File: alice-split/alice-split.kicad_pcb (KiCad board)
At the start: 2 copper layers, 0 parts

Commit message: Drew curved traces instead of the usual defaults. Not sure I like it. Going to branch and try again.
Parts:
- added D1: D_Small, Diode_SMD:D_1206_3216Metric, B.Cu at (83.8, 53.8)
- added D10: D_Small, Diode_SMD:D_1206_3216Metric, B.Cu at (183.4, 59.9)
- added D11: D_Small, Diode_SMD:D_1206_3216Metric, B.Cu at (164.6, 55.9)
- added D12: D_Small, Diode_SMD:D_1206_3216Metric, B.Cu at (144.8, 53.3)
- added D13: D_Small, Diode_SMD:D_1206_3216Metric, B.Cu at (126.0, 55.9)
- added D14: D_Small, Diode_SMD:D_1206_3216Metric, B.Cu at (107.2, 55.9)
- added D15: D_Small, Diode_SMD:D_1206_3216Metric, B.Cu at (107.7, 74.7)
- added D16: D_Small, Diode_SMD:D_1206_3216Metric, B.Cu at (131.1, 75.2)
- added D17: D_Small, Diode_SMD:D_1206_3216Metric, B.Cu at (151.9, 72.4)
- added D18: D_Small, Diode_SMD:D_1206_3216Metric, B.Cu at (170.4, 76.5)
- added D19: D_Small, Diode_SMD:D_1206_3216Metric, B.Cu at (189.0, 80.3)
- added D2: D_Small, Diode_SMD:D_1206_3216Metric, F.Cu at (-86.4, 63.0)
- added D20: D_Small, Diode_SMD:D_1206_3216Metric, B.Cu at (207.8, 84.3)
- added D21: D_Small, Diode_SMD:D_1206_3216Metric, B.Cu at (100.8, 94.0)
- added D22: D_Small, Diode_SMD:D_1206_3216Metric, B.Cu at (131.8, 93.7)
- added D23: D_Small, Diode_SMD:D_1206_3216Metric, B.Cu at (153.2, 92.5)
- added D24: D_Small, Diode_SMD:D_1206_3216Metric, B.Cu at (170.9, 95.5)
- added D25: D_Small, Diode_SMD:D_1206_3216Metric, B.Cu at (189.7, 99.8)
- added D26: D_Small, Diode_SMD:D_1206_3216Metric, B.Cu at (208.5, 104.1)
- added D27: D_Small, Diode_SMD:D_1206_3216Metric, B.Cu at (114.8, 103.1)
- added D28: D_Small, Diode_SMD:D_1206_3216Metric, B.Cu at (137.4, 112.8)
- added D29: D_Small, Diode_SMD:D_1206_3216Metric, B.Cu at (157.7, 112.8)
- added D3: D_Small, Diode_SMD:D_1206_3216Metric, F.Cu at (-79.1, 141.7)
- added D30: D_Small, Diode_SMD:D_1206_3216Metric, B.Cu at (176.5, 116.6)
- added D31: D_Small, Diode_SMD:D_1206_3216Metric, B.Cu at (195.1, 120.7)
- added D32: D_Small, Diode_SMD:D_1206_3216Metric, B.Cu at (213.9, 124.5)
- added D33: D_Small, Diode_SMD:D_1206_3216Metric, B.Cu at (99.3, 131.8)
- added D34: D_Small, Diode_SMD:D_1206_3216Metric, B.Cu at (118.1, 131.8)
- added D35: D_Small, Diode_SMD:D_1206_3216Metric, B.Cu at (153.2, 132.6)
- added D36: D_Small, Diode_SMD:D_1206_3216Metric, B.Cu at (174.2, 136.9)
- added D37: D_Small, Diode_SMD:D_1206_3216Metric, B.Cu at (217.9, 145.0)
- added D4: D_Small, Diode_SMD:D_1206_3216Metric, F.Cu at (-79.1, 145.1)
- added D5: D_Small, Diode_SMD:D_1206_3216Metric, F.Cu at (-79.1, 148.5)
- added D6: D_Small, Diode_SMD:D_1206_3216Metric, F.Cu at (-79.1, 151.9)
- added D7: D_Small, Diode_SMD:D_1206_3216Metric, F.Cu at (-77.2, 120.4)
- added D8: D_Small, Diode_SMD:D_1206_3216Metric, B.Cu at (221.0, 67.6)
- added D9: D_Small, Diode_SMD:D_1206_3216Metric, B.Cu at (202.7, 64.0)
- added SW38: SW_PUSH-MX_W_LED, SofleRGB:SK6812MINI_and_cherry, F.Cu at (-251.0, 57.5)
- added SW39: SW_PUSH-MX_W_LED, SofleRGB:SK6812MINI_and_cherry, F.Cu at (-210.7, 117.3)
- added SW40: SW_PUSH-MX_W_LED, SofleRGB:SK6812MINI_and_cherry, F.Cu at (-268.0, 89.5)
- added SW41: SW_PUSH-MX_W_LED, SofleRGB:SK6812MINI_and_cherry, F.Cu at (-329.3, 121.5)
- added SW42: SW_PUSH-MX_W_LED, SofleRGB:SK6812MINI_and_cherry, F.Cu at (-329.3, 137.0)
- added SW43: SW_PUSH-MX_W_LED, SofleRGB:SK6812MINI_and_cherry, F.Cu at (-329.3, 152.5)
- added SW44: SW_PUSH-MX_W_LED, SofleRGB:SK6812MINI_and_cherry, F.Cu at (-353.4, 162.8)
- added SW45: SW_PUSH-MX_W_LED, SofleRGB:SK6812MINI_and_cherry, F.Cu at (-353.4, 178.3)
- added SW46: SW_PUSH-MX_W_LED, SofleRGB:SK6812MINI_and_cherry, F.Cu at (-353.4, 193.8)
- added SW47: SW_PUSH-MX_W_LED, SofleRGB:SK6812MINI_and_cherry, F.Cu at (-353.4, 209.3)
- added SW48: SW_PUSH-MX_W_LED, SofleRGB:SK6812MINI_and_cherry, F.Cu at (-353.4, 224.8)
- added SW49: SW_PUSH-MX_W_LED, SofleRGB:SK6812MINI_and_cherry, F.Cu at (-198.6, 76.2)
- added SW50: SW_PUSH-MX_W_LED, SofleRGB:SK6812MINI_and_cherry, F.Cu at (-299.1, 134.0)
- added SW51: SW_PUSH-MX_W_LED, SofleRGB:SK6812MINI_and_cherry, F.Cu at (-299.1, 149.5)
- added SW52: SW_PUSH-MX_W_LED, SofleRGB:SK6812MINI_and_cherry, F.Cu at (-299.1, 165.0)
- added SW53: SW_PUSH-MX_W_LED, SofleRGB:SK6812MINI_and_cherry, F.Cu at (-299.1, 180.5)
- added SW54: SW_PUSH-MX_W_LED, SofleRGB:SK6812MINI_and_cherry, F.Cu at (-299.1, 196.0)
- added SW55: SW_PUSH-MX_W_LED, SofleRGB:SK6812MINI_and_cherry, F.Cu at (-299.1, 211.5)
- added SW56: SW_PUSH-MX_W_LED, SofleRGB:SK6812MINI_and_cherry, F.Cu at (-299.1, 227.0)
- added SW57: SW_PUSH-MX_W_LED, SofleRGB:SK6812MINI_and_cherry, F.Cu at (-299.1, 242.5)
- added SW58: SW_PUSH-MX_W_LED, SofleRGB:SK6812MINI_and_cherry, F.Cu at (-299.1, 258.0)
- added SW59: SW_PUSH-MX_W_LED, SofleRGB:SK6812MINI_and_cherry, F.Cu at (-299.1, 273.5)
- added SW60: SW_PUSH-MX_W_LED, SofleRGB:SK6812MINI_and_cherry, F.Cu at (-281.8, 118.5)
- added SW61: SW_PUSH-MX_W_LED, SofleRGB:SK6812MINI_and_cherry, F.Cu at (-281.8, 134.0)
- added SW62: SW_PUSH-MX_W_LED, SofleRGB:SK6812MINI_and_cherry, F.Cu at (-281.8, 149.5)
- added SW63: SW_PUSH-MX_W_LED, SofleRGB:SK6812MINI_and_cherry, F.Cu at (-281.8, 165.0)
- added SW64: SW_PUSH-MX_W_LED, SofleRGB:SK6812MINI_and_cherry, F.Cu at (-281.8, 180.5)
- added SW65: SW_PUSH-MX_W_LED, SofleRGB:SK6812MINI_and_cherry, F.Cu at (-281.8, 196.0)
- added SW66: SW_PUSH-MX_W_LED, SofleRGB:SK6812MINI_and_cherry, F.Cu at (-281.8, 211.5)
- added SW67: SW_PUSH-MX_W_LED, SofleRGB:SK6812MINI_and_cherry, F.Cu at (-281.8, 227.0)
- added SW68: SW_PUSH-MX_W_LED, SofleRGB:SK6812MINI_and_cherry, F.Cu at (-281.8, 242.5)
- added SW69: SW_PUSH-MX_W_LED, SofleRGB:SK6812MINI_and_cherry, F.Cu at (-281.8, 258.0)
- added SW70: SW_PUSH-MX_W_LED, SofleRGB:SK6812MINI_and_cherry, F.Cu at (-281.8, 273.5)
- added SW71: SW_PUSH-MX_W_LED, SofleRGB:SK6812MINI_and_cherry, F.Cu at (-264.5, 118.5)
- added SW72: SW_PUSH-MX_W_LED, SofleRGB:SK6812MINI_and_cherry, F.Cu at (-264.5, 134.0)
- added SW73: SW_PUSH-MX_W_LED, SofleRGB:SK6812MINI_and_cherry, F.Cu at (-264.5, 149.5)
- added SW74: SW_PUSH-MX_W_LED, SofleRGB:SK6812MINI_and_cherry, F.Cu at (-264.5, 165.0)
- added SW75: SW_PUSH-MX_W_LED, SofleRGB:SK6812MINI_and_cherry, F.Cu at (-264.5, 180.5)
- added SW76: SW_PUSH-MX_W_LED, SofleRGB:SK6812MINI_and_cherry, F.Cu at (-264.5, 196.0)
- added SW77: SW_PUSH-MX_W_LED, SofleRGB:SK6812MINI_and_cherry, F.Cu at (-264.5, 211.5)
- added SW78: SW_PUSH-MX_W_LED, SofleRGB:SK6812MINI_and_cherry, F.Cu at (-264.5, 227.0)
- added SW79: SW_PUSH-MX_W_LED, SofleRGB:SK6812MINI_and_cherry, F.Cu at (-264.5, 242.5)
- added SW80: SW_PUSH-MX_W_LED, SofleRGB:SK6812MINI_and_cherry, F.Cu at (-264.5, 258.0)
- added SW81: SW_PUSH-MX_W_LED, SofleRGB:SK6812MINI_and_cherry, F.Cu at (-192.9, 259.5)
- added SW82: SW_PUSH-MX_W_LED, SofleRGB:SK6812MINI_and_cherry, F.Cu at (-228.0, 130.5)
- added SW83: SW_PUSH-MX_W_LED, SofleRGB:SK6812MINI_and_cherry, F.Cu at (-228.0, 146.0)
- added SW84: SW_PUSH-MX_W_LED, SofleRGB:SK6812MINI_and_cherry, F.Cu at (-228.0, 161.5)
- added SW85: SW_PUSH-MX_W_LED, SofleRGB:SK6812MINI_and_cherry, F.Cu at (-228.0, 177.0)
- added SW86: SW_PUSH-MX_W_LED, SofleRGB:SK6812MINI_and_cherry, F.Cu at (-228.0, 192.5)
- added SW87: SW_PUSH-MX_W_LED, SofleRGB:SK6812MINI_and_cherry, F.Cu at (-228.0, 208.0)
- added SW88: SW_PUSH-MX_W_LED, SofleRGB:SK6812MINI_and_cherry, F.Cu at (-228.0, 223.5)
- added SW89: SW_PUSH-MX_W_LED, SofleRGB:SK6812MINI_and_cherry, F.Cu at (-228.0, 239.0)
- added SW_1: SW_PUSH-MX_W_LED, SofleRGB:SK6812MINI_and_cherry, F.Cu at (134.0, 54.4)
- added SW_2: SW_PUSH-MX_W_LED, SofleRGB:SK6812MINI_and_cherry, F.Cu at (152.6, 52.2)
- added SW_3: SW_PUSH-MX_W_LED, SofleRGB:SK6812MINI_and_cherry, F.Cu at (173.1, 56.2)
- added SW_4: SW_PUSH-MX_W_LED, SofleRGB:SK6812MINI_and_cherry, F.Cu at (191.8, 60.2)
- added SW_5: SW_PUSH-MX_W_LED, SofleRGB:SK6812MINI_and_cherry, F.Cu at (210.4, 64.1)
- added SW_6: SW_PUSH-MX_W_LED, SofleRGB:SK6812MINI_and_cherry, F.Cu at (229.0, 68.1)
- added SW_A1: SW_PUSH-MX_W_LED, SofleRGB:SK6812MINI_and_cherry, F.Cu at (140.0, 92.5)
- added SW_B_L1: SW_PUSH-MX_W_LED, SofleRGB:SK6812MINI_and_cherry, F.Cu at (221.8, 125.0)
- added SW_C1: SW_PUSH-MX_W_LED, SofleRGB:SK6812MINI_and_cherry, F.Cu at (184.6, 117.0)
- added SW_CAPS1: SW_PUSH-MX_W_LED, SofleRGB:SK6812MINI_and_cherry, F.Cu at (109.1, 92.5)
- added SW_CTRL_L1: SW_PUSH-MX_W_LED, SofleRGB:SK6812MINI_and_cherry, F.Cu at (107.3, 130.6)
- added SW_D1: SW_PUSH-MX_W_LED, SofleRGB:SK6812MINI_and_cherry, F.Cu at (178.8, 96.0)
- added SW_E1: SW_PUSH-MX_W_LED, SofleRGB:SK6812MINI_and_cherry, F.Cu at (178.5, 76.8)
- added SW_ESC1: SW_PUSH-MX_W_LED, SofleRGB:SK6812MINI_and_cherry, F.Cu at (91.9, 52.2)
- added SW_F1: SW_PUSH-MX_W_LED, SofleRGB:SK6812MINI_and_cherry, F.Cu at (-113.1, -344.2)
- added SW_F2: SW_PUSH-MX_W_LED, SofleRGB:SK6812MINI_and_cherry, F.Cu at (-53.7, -218.7)
- added SW_F3: SW_PUSH-MX_W_LED, SofleRGB:SK6812MINI_and_cherry, F.Cu at (29.0, -292.6)
- added SW_F4: SW_PUSH-MX_W_LED, SofleRGB:SK6812MINI_and_cherry, F.Cu at (60.5, -290.6)
- added SW_F5: SW_PUSH-MX_W_LED, SofleRGB:SK6812MINI_and_cherry, F.Cu at (91.4, -280.9)
- added SW_F6: SW_PUSH-MX_W_LED, SofleRGB:SK6812MINI_and_cherry, F.Cu at (59.4, -248.4)
- added SW_F7: SW_PUSH-MX_W_LED, SofleRGB:SK6812MINI_and_cherry, F.Cu at (-59.8, -186.2)
- added SW_F8: SW_PUSH-MX_W_LED, SofleRGB:SK6812MINI_and_cherry, F.Cu at (197.6, 100.1)
- added SW_FN1: SW_PUSH-MX_W_LED, SofleRGB:SK6812MINI_and_cherry, F.Cu at (225.9, 145.3)
- added SW_G1: SW_PUSH-MX_W_LED, SofleRGB:SK6812MINI_and_cherry, F.Cu at (216.4, 104.3)
- added SW_M1: SW_PUSH-MX_W_LED, SofleRGB:SK6812MINI_and_cherry, F.Cu at (-15.4, 25.5)
- added SW_M2: SW_PUSH-MX_W_LED, SofleRGB:SK6812MINI_and_cherry, F.Cu at (-15.4, 41.0)
- added SW_MOD_L1: SW_PUSH-MX_W_LED, SofleRGB:SK6812MINI_and_cherry, F.Cu at (161.1, 133.0)
- added SW_OPT1: SW_PUSH-MX_W_LED, SofleRGB:SK6812MINI_and_cherry, F.Cu at (126.4, 130.6)
- added SW_Q1: SW_PUSH-MX_W_LED, SofleRGB:SK6812MINI_and_cherry, F.Cu at (139.3, 73.4)
- added SW_R1: SW_PUSH-MX_W_LED, SofleRGB:SK6812MINI_and_cherry, F.Cu at (197.1, 80.8)
- added SW_S1: SW_PUSH-MX_W_LED, SofleRGB:SK6812MINI_and_cherry, F.Cu at (161.0, 93.0)
- added SW_SHIFT_L1: SW_PUSH-MX_W_LED, SofleRGB:SK6812MINI_and_cherry, F.Cu at (114.5, 111.5)
- added SW_SPC_L1: SW_PUSH-MX_W_LED, SofleRGB:SK6812MINI_and_cherry, F.Cu at (195.5, 138.9)
- added SW_T1: SW_PUSH-MX_W_LED, SofleRGB:SK6812MINI_and_cherry, F.Cu at (215.8, 84.7)
- added SW_TAB1: SW_PUSH-MX_W_LED, SofleRGB:SK6812MINI_and_cherry, F.Cu at (115.5, 73.4)
- added SW_TILDE1: SW_PUSH-MX_W_LED, SofleRGB:SK6812MINI_and_cherry, F.Cu at (115.0, 54.4)
- added SW_V1: SW_PUSH-MX_W_LED, SofleRGB:SK6812MINI_and_cherry, F.Cu at (203.1, 121.0)
- added SW_W1: SW_PUSH-MX_W_LED, SofleRGB:SK6812MINI_and_cherry, F.Cu at (159.8, 72.8)
- added SW_X1: SW_PUSH-MX_W_LED, SofleRGB:SK6812MINI_and_cherry, F.Cu at (165.9, 113.1)
- added SW_Z1: SW_PUSH-MX_W_LED, SofleRGB:SK6812MINI_and_cherry, F.Cu at (145.4, 111.5)
- added U1: Sparkfun_Pro_Micro, Keebio-Parts:ArduinoProMicro, B.Cu at (230.4, 47.2)
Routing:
- net Net-(D16-A): track 0.00 -> 3.47 mm
- net Net-(D1-A): track 0.00 -> 3.24 mm
- net Net-(D10-A): track 0.00 -> 3.22 mm
- net Net-(D21-A): track 0.00 -> 3.21 mm
- net Net-(D11-A): track 0.00 -> 3.17 mm
- net Net-(D13-A): track 0.00 -> 3.09 mm
- net Net-(D26-A): track 0.00 -> 3.06 mm
- net Net-(D9-A): track 0.00 -> 3.03 mm
- net Net-(D29-A): track 0.00 -> 3.03 mm
- net Net-(D14-A): track 0.00 -> 3.01 mm
- net Net-(D37-A): track 0.00 -> 2.98 mm
- net Net-(D25-A): track 0.00 -> 2.97 mm
- net Net-(D34-A): track 0.00 -> 2.94 mm
- net Net-(D18-A): track 0.00 -> 2.94 mm
- net Net-(D31-A): track 0.00 -> 2.94 mm
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
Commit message: Redid the traces but with the usual 45 degree traces. Looks nicer, made more progress.
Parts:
- moved SW_F1 368.9 mm to (-381.5, -91.0)
- moved SW_F3 368.9 mm to (-239.4, -39.4)
- moved SW_F4 368.9 mm to (-207.9, -37.4)
- moved SW_F2 368.9 mm to (-322.0, 34.5)
- moved SW_F5 368.9 mm to (-176.9, -27.7)
- moved SW_F6 368.9 mm to (-208.9, 4.80)
- moved SW_F7 368.9 mm to (-328.1, 67.0)
- moved SW_TILDE1 140.1 mm to (-18.0, 10.3)
- moved D14 132.7 mm to (-21.6, 23.9)
- moved SW_M1 112.9 mm to (87.8, 71.3)
- moved SW_M2 110.7 mm to (83.7, 90.4)
- moved D1 23.1 mm to (106.9, 56.0)
- moved SW_ESC1 23.1 mm to (115.0, 54.4)
- moved D36 13.4 mm to (187.5, 139.2), turned to 78 degrees
- moved U1 0.57 mm to (230.9, 47.0)
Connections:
- D1 pad 1: ROW5 -> ROW4
- D14 pad 1: ROW4 -> unconnected-(D14-K-Pad1)
- D14 pad 2: Net-(D14-A) -> unconnected-(D14-A-Pad2)
- D2 pad 1: ROW5 -> unconnected-(D2-K-Pad1)
- D3 pad 1: ROW5 -> unconnected-(D3-K-Pad1)
- D4 pad 1: ROW5 -> unconnected-(D4-K-Pad1)
- D5 pad 1: ROW5 -> unconnected-(D5-K-Pad1)
- D6 pad 1: ROW5 -> unconnected-(D6-K-Pad1)
- D7 pad 1: ROW5 -> unconnected-(D7-K-Pad1)
- SW_E1 pad 4: Net-(SW_6B-DIN) -> VDD
- SW_ESC1 pad 3: Net-(SW_ESC1B-DIN) -> Net-(SW_1B-DOUT)
- SW_ESC1 pad 6: COL15 -> COL14
- SW_F1 pad 1: Net-(SW_ESC1B-DIN) -> unconnected-(SW_F1B-DOUT-Pad1)
- SW_F1 pad 2: VCC -> unconnected-(SW_F1B-VSS-Pad2)
- SW_F1 pad 4: VDD -> unconnected-(SW_F1B-VDD-Pad4)
- SW_F1 pad 6: COL13 -> unconnected-(SW_F1-Pad6)
- SW_F2 pad 2: VCC -> unconnected-(SW_F2B-VSS-Pad2)
- SW_F2 pad 4: VDD -> unconnected-(SW_F2B-VDD-Pad4)
- SW_F2 pad 6: COL12 -> unconnected-(SW_F2-Pad6)
- SW_F3 pad 2: VCC -> unconnected-(SW_F3B-VSS-Pad2)
- SW_F3 pad 4: VDD -> unconnected-(SW_F3B-VDD-Pad4)
- SW_F3 pad 6: COL11 -> unconnected-(SW_F3-Pad6)
- SW_F4 pad 2: VCC -> unconnected-(SW_F4B-VSS-Pad2)
- SW_F4 pad 4: VDD -> unconnected-(SW_F4B-VDD-Pad4)
- SW_F4 pad 6: COL10 -> unconnected-(SW_F4-Pad6)
- SW_F5 pad 2: VCC -> unconnected-(SW_F5B-VSS-Pad2)
- SW_F5 pad 4: VDD -> unconnected-(SW_F5B-VDD-Pad4)
- SW_F5 pad 6: COL9 -> unconnected-(SW_F5-Pad6)
- SW_F6 pad 2: VCC -> unconnected-(SW_F6B-VSS-Pad2)
- SW_F6 pad 3: Net-(SW_F6B-DIN) -> unconnected-(SW_F6B-DIN-Pad3)
- SW_F6 pad 4: VDD -> unconnected-(SW_F6B-VDD-Pad4)
- SW_F6 pad 6: COL8 -> unconnected-(SW_F6-Pad6)
- SW_Q1 pad 4: Net-(SW_6B-DIN) -> VDD
- SW_R1 pad 4: Net-(SW_6B-DIN) -> VDD
- SW_TAB1 pad 4: Net-(SW_6B-DIN) -> VDD
- SW_TILDE1 pad 1: Net-(SW_F6B-DIN) -> unconnected-(SW_TILDE1B-DOUT-Pad1)
- SW_TILDE1 pad 2: VCC -> unconnected-(SW_TILDE1B-VSS-Pad2)
- SW_TILDE1 pad 3: Net-(SW_1B-DOUT) -> unconnected-(SW_TILDE1B-DIN-Pad3)
- SW_TILDE1 pad 4: VDD -> unconnected-(SW_TILDE1B-VDD-Pad4)
- SW_TILDE1 pad 5: Net-(D14-A) -> unconnected-(SW_TILDE1-Pad5)
- SW_TILDE1 pad 6: COL14 -> unconnected-(SW_TILDE1-Pad6)
- SW_W1 pad 4: Net-(SW_6B-DIN) -> VDD
- U1 pad 10: ROW4 -> unconnected-(U1-D7-Pad10)
- U1 pad 11: ROW5 -> unconnected-(U1-D8/A8-Pad11)
- U1 pad 12: ROW6 -> unconnected-(U1-~D9/A9-Pad12)
- U1 pad 13: COL15 -> unconnected-(U1-~D10/A10-Pad13)
- U1 pad 23: VDD -> unconnected-(U1-GND-Pad23)
- U1 pad 3: unconnected-(U1-GND-Pad3) -> VDD
- U1 pad 4: unconnected-(U1-GND-Pad4) -> VDD
- U1 pad 5: unconnected-(U1-D2-Pad5) -> ROW0
- U1 pad 6: ROW0 -> ROW1
- U1 pad 7: ROW1 -> ROW2
- U1 pad 8: ROW2 -> ROW3
- U1 pad 9: ROW3 -> ROW4
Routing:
- net VDD: track 0.00 -> 675.7 mm, vias 0 -> 31
- net VCC: track 0.00 -> 663.5 mm
- net COL14: track 0.00 -> 222.5 mm, vias 0 -> 5
- net ROW1: track 0.00 -> 195.8 mm
- net COL13: track 0.00 -> 194.1 mm, vias 0 -> 5
- net ROW2: track 0.00 -> 186.7 mm
- net ROW3: track 0.00 -> 170.7 mm
- net ROW4: track 0.00 -> 162.8 mm
- net COL11: track 0.00 -> 162.3 mm, vias 0 -> 5
- net Net-(SW_G1B-DIN): track 0.00 -> 158.5 mm
- net Net-(SW_6B-DIN): track 0.00 -> 151.4 mm
- net Net-(SW_B_L1B-DIN): track 0.00 -> 146.3 mm
- net COL12: track 0.00 -> 144.9 mm, vias 0 -> 4
- net Net-(SW_CAPS1B-DOUT): track 0.00 -> 143.5 mm
- net COL10: track 0.00 -> 135.0 mm, vias 0 -> 5
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
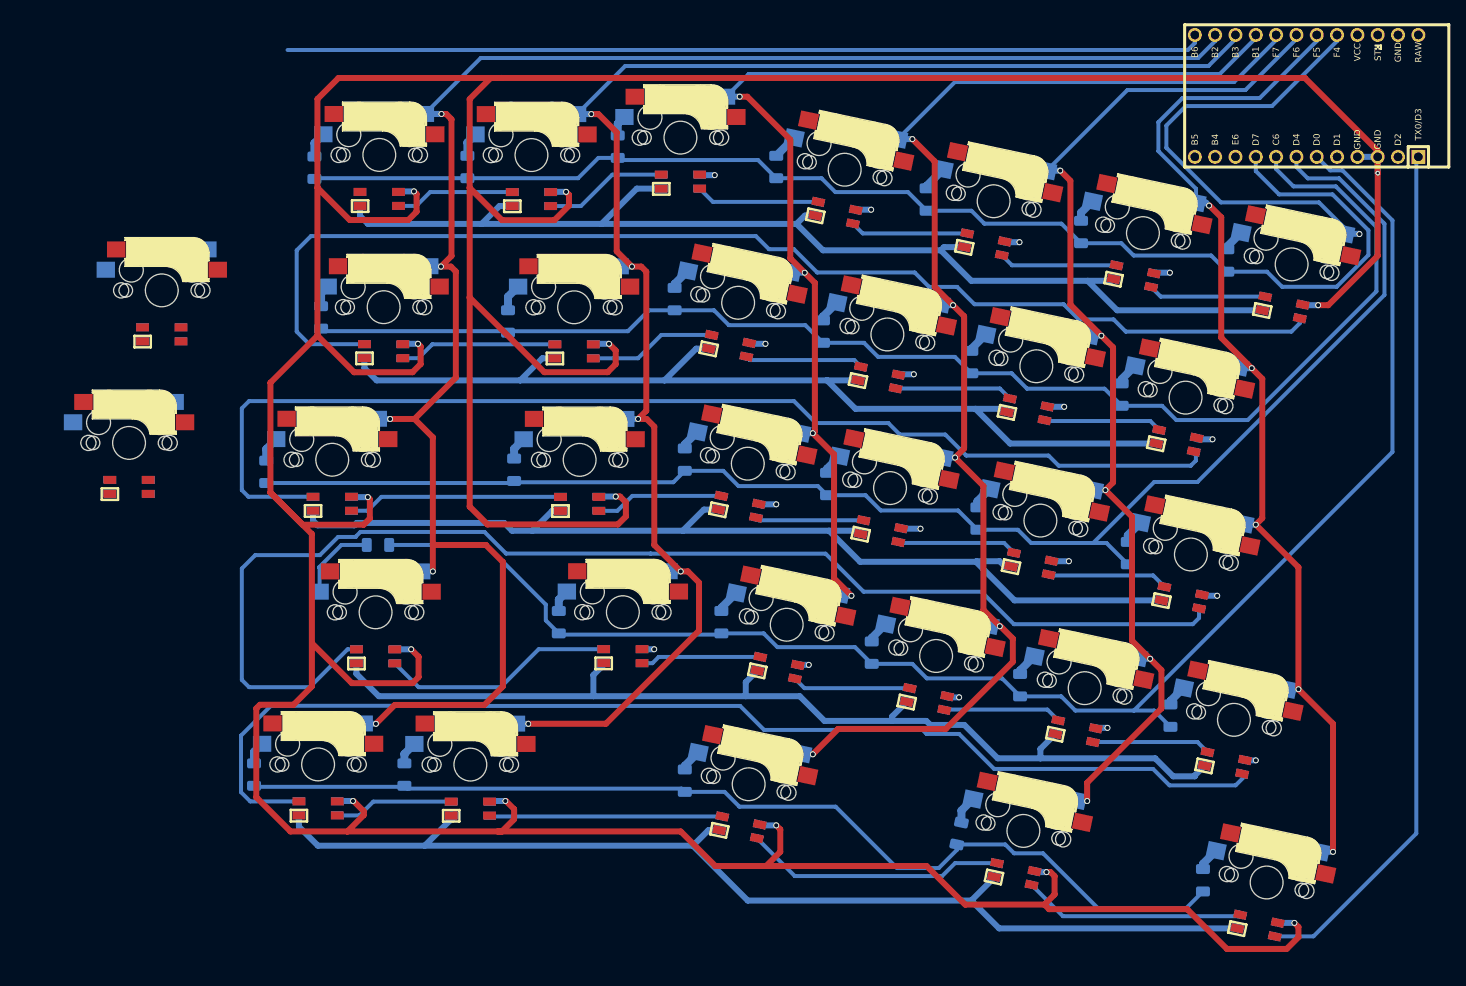
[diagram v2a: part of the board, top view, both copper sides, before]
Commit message: Added encoder and macro keys. Whole lefthand side is wired. Needs another review.
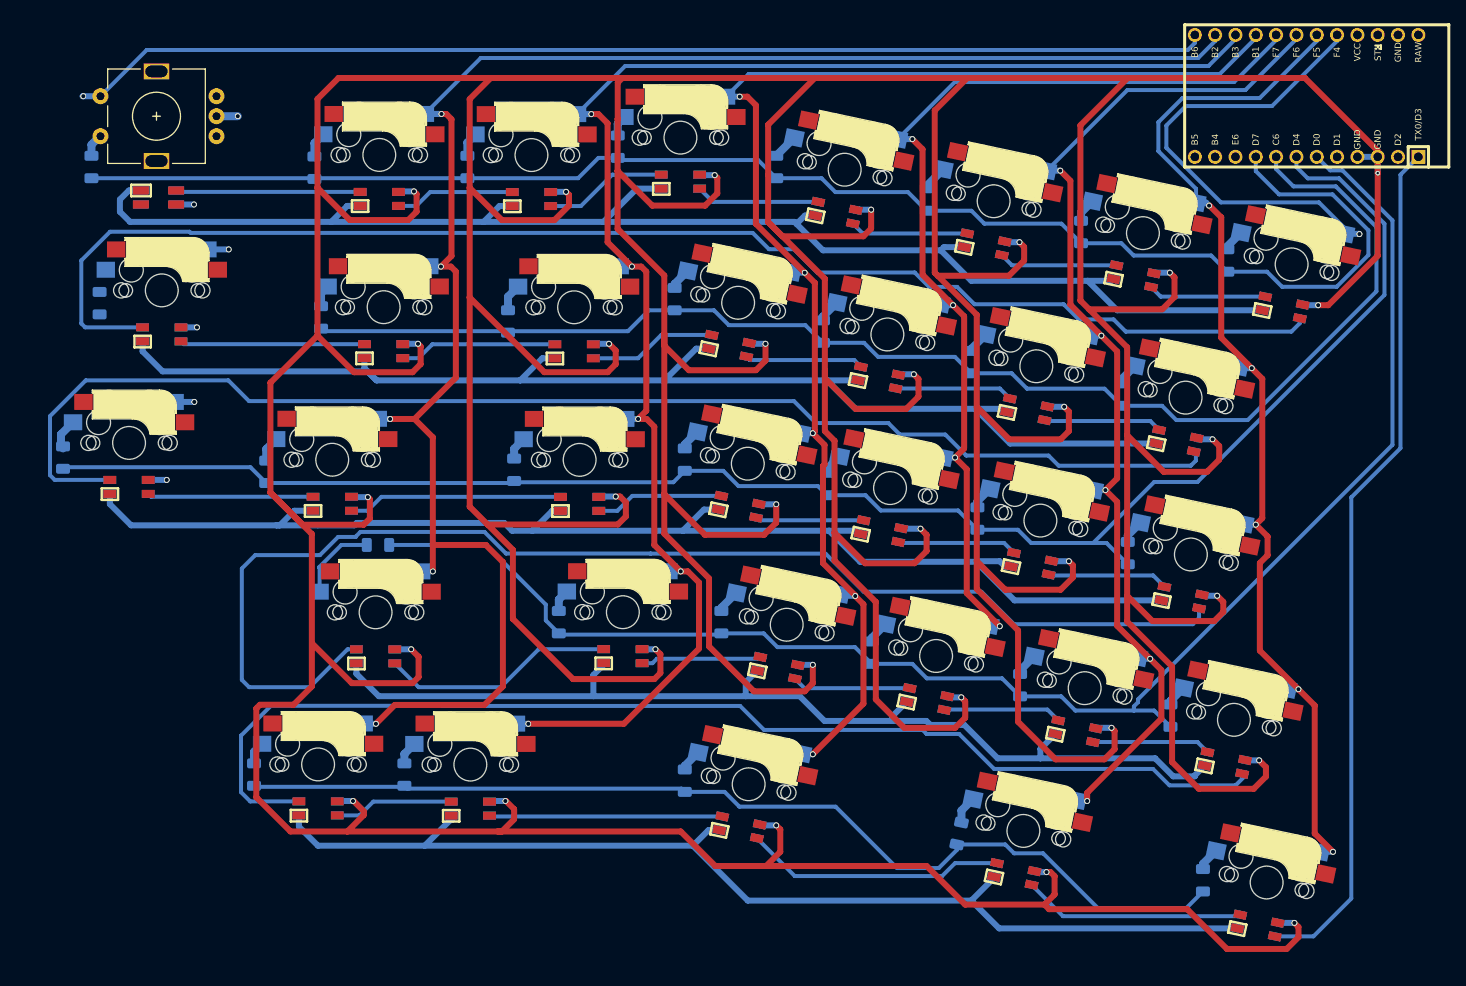
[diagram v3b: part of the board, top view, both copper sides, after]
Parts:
- added D38: D_Small, Diode_SMD:D_1206_3216Metric, B.Cu at (79.0, 55.9)
- added D39: D_Small, Diode_SMD:D_1206_3216Metric, B.Cu at (80.0, 72.9)
- added D40: D_Small, Diode_SMD:D_1206_3216Metric, B.Cu at (75.4, 92.2)
- added D41: LED_sk2812_SM, SofleRGB:SK6812MINI_underglow_dev, F.Cu at (87.4, 59.7)
- added SW1: RotaryEncoder_Switch, SofleRGB:RotaryEncoder_Alps_EC11E-Switch_Vertical_H20mm-keebio_modified, F.Cu at (87.1, 49.5)
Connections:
- SW_ESC1 pad 1: unconnected-(SW_ESC1B-DOUT-Pad1) -> Net-(D41-DIN)
- SW_M1 pad 1: unconnected-(SW_M1B-DOUT-Pad1) -> Net-(SW_6B-DIN)
- SW_M1 pad 2: unconnected-(SW_M1B-VSS-Pad2) -> VCC
- SW_M1 pad 3: unconnected-(SW_M1B-DIN-Pad3) -> Net-(SW_M1B-DIN)
- SW_M1 pad 4: unconnected-(SW_M1B-VDD-Pad4) -> VDD
- SW_M1 pad 5: unconnected-(SW_M1-Pad5) -> Net-(D39-A)
- SW_M1 pad 6: unconnected-(SW_M1-Pad6) -> COL15
- SW_M2 pad 1: unconnected-(SW_M2B-DOUT-Pad1) -> Net-(SW_M2B-DOUT)
- SW_M2 pad 2: unconnected-(SW_M2B-VSS-Pad2) -> VCC
- SW_M2 pad 3: unconnected-(SW_M2B-DIN-Pad3) -> Net-(SW_CAPS1B-DOUT)
- SW_M2 pad 4: unconnected-(SW_M2B-VDD-Pad4) -> VDD
- SW_M2 pad 5: unconnected-(SW_M2-Pad5) -> Net-(D40-A)
- SW_M2 pad 6: unconnected-(SW_M2-Pad6) -> COL15
- SW_MOD_L1 pad 6: COL11 -> COL12
- SW_T1 pad 3: Net-(SW_CAPS1B-DOUT) -> Net-(SW_M2B-DOUT)
- SW_TAB1 pad 1: Net-(SW_6B-DIN) -> Net-(SW_M1B-DIN)
- U1 pad 11: unconnected-(U1-D8/A8-Pad11) -> ENCA
- U1 pad 12: unconnected-(U1-~D9/A9-Pad12) -> ENCB
- U1 pad 13: unconnected-(U1-~D10/A10-Pad13) -> COL15
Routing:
- net VDD: track 675.7 -> 1335.6 mm, vias 31 -> 35
- net Net-(SW_M2B-DOUT): track 0.00 -> 165.7 mm
- net COL15: track 0.00 -> 147.9 mm, vias 0 -> 3
- net Net-(SW_CAPS1B-DOUT): track 143.5 -> 20.7 mm
- net unconnected-(U1-~D10/A10-Pad13): track 114.8 -> 0.00 mm
- net VCC: track 663.5 -> 764.4 mm
- net COL11: track 162.3 -> 125.8 mm, vias 5 -> 4
- net ROW4: track 162.8 -> 190.7 mm
- net ROW2: track 186.7 -> 213.0 mm
- net COL12: track 144.9 -> 170.1 mm, vias 4 -> 5
- net Net-(SW_6B-DIN): track 151.4 -> 175.8 mm
- net Net-(SW_M1B-DIN): track 0.00 -> 23.1 mm
- net Net-(D41-DIN): track 0.00 -> 23.1 mm
- net Net-(D40-A): track 0.00 -> 4.00 mm
- net ENC_S2: track 0.00 -> 2.96 mm
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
